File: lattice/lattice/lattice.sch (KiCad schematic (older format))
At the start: 108 parts, among them J1 AudioJack2, J10 AudioJack2, J11 AudioJack2, J12 AudioJack2, J13 AudioJack2, J14 AudioJack2, J15 AudioJack2, J16 Conn_02x05_Odd_Even, J17 Conn_01x10, J18 Conn_01x10, J19 Conn_01x08, J2 AudioJack2, J20 Conn_01x08, J21 Conn_01x07, J22 Conn_01x07, J23 Conn_01x07, J24 Conn_01x07, J3 AudioJack2, J4 AudioJack2, J5 AudioJack2, J6 AudioJack2, J7 AudioJack2, J8 AudioJack2, J9 Conn_02x08_Odd_Even, Q1 BC548, Q2 BC548, SW1 LP4OA1PBCT, U1 MCP6002-xP, U2 MCP6002-xP, U3 MCP6002-xP, U5 6N138, U6 LM4040LP-5, U7 74HC595

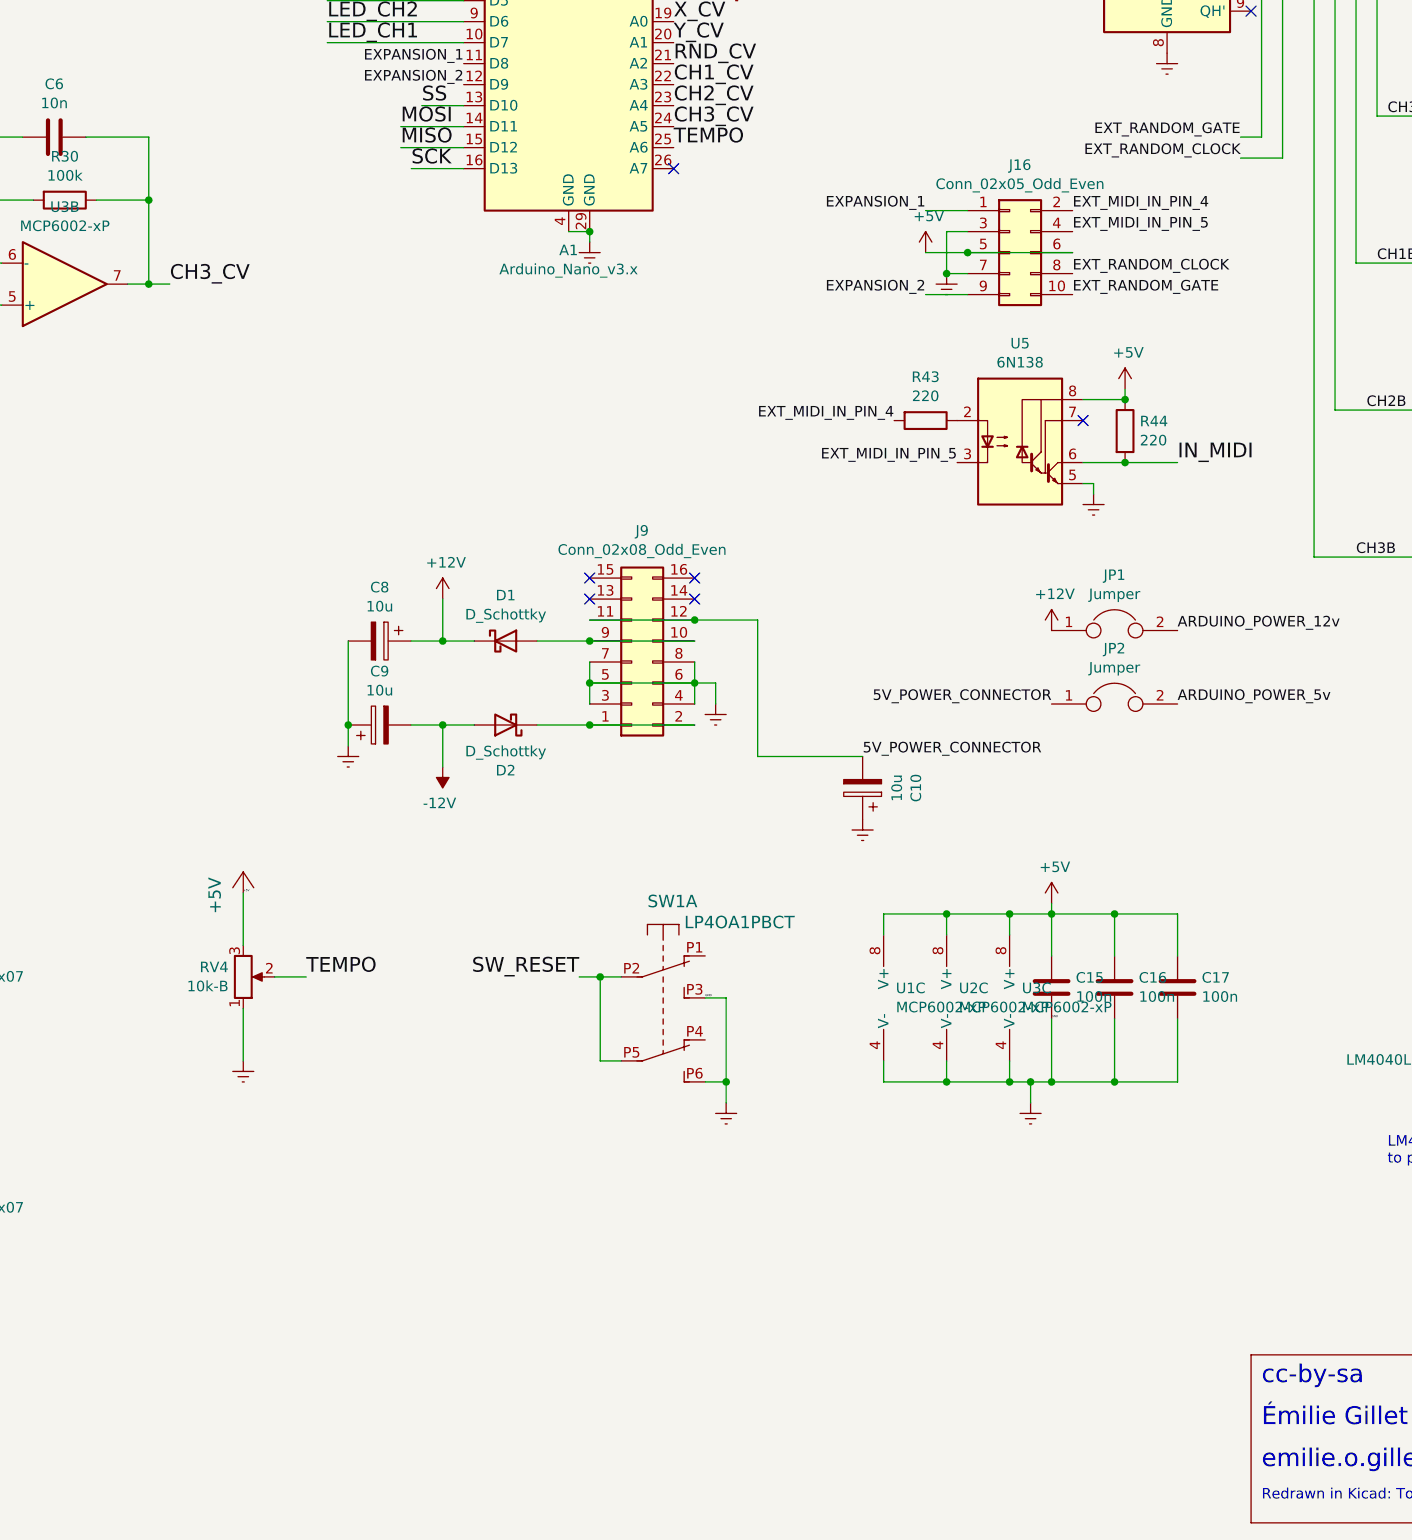
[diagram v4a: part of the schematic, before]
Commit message: Adding expansion board
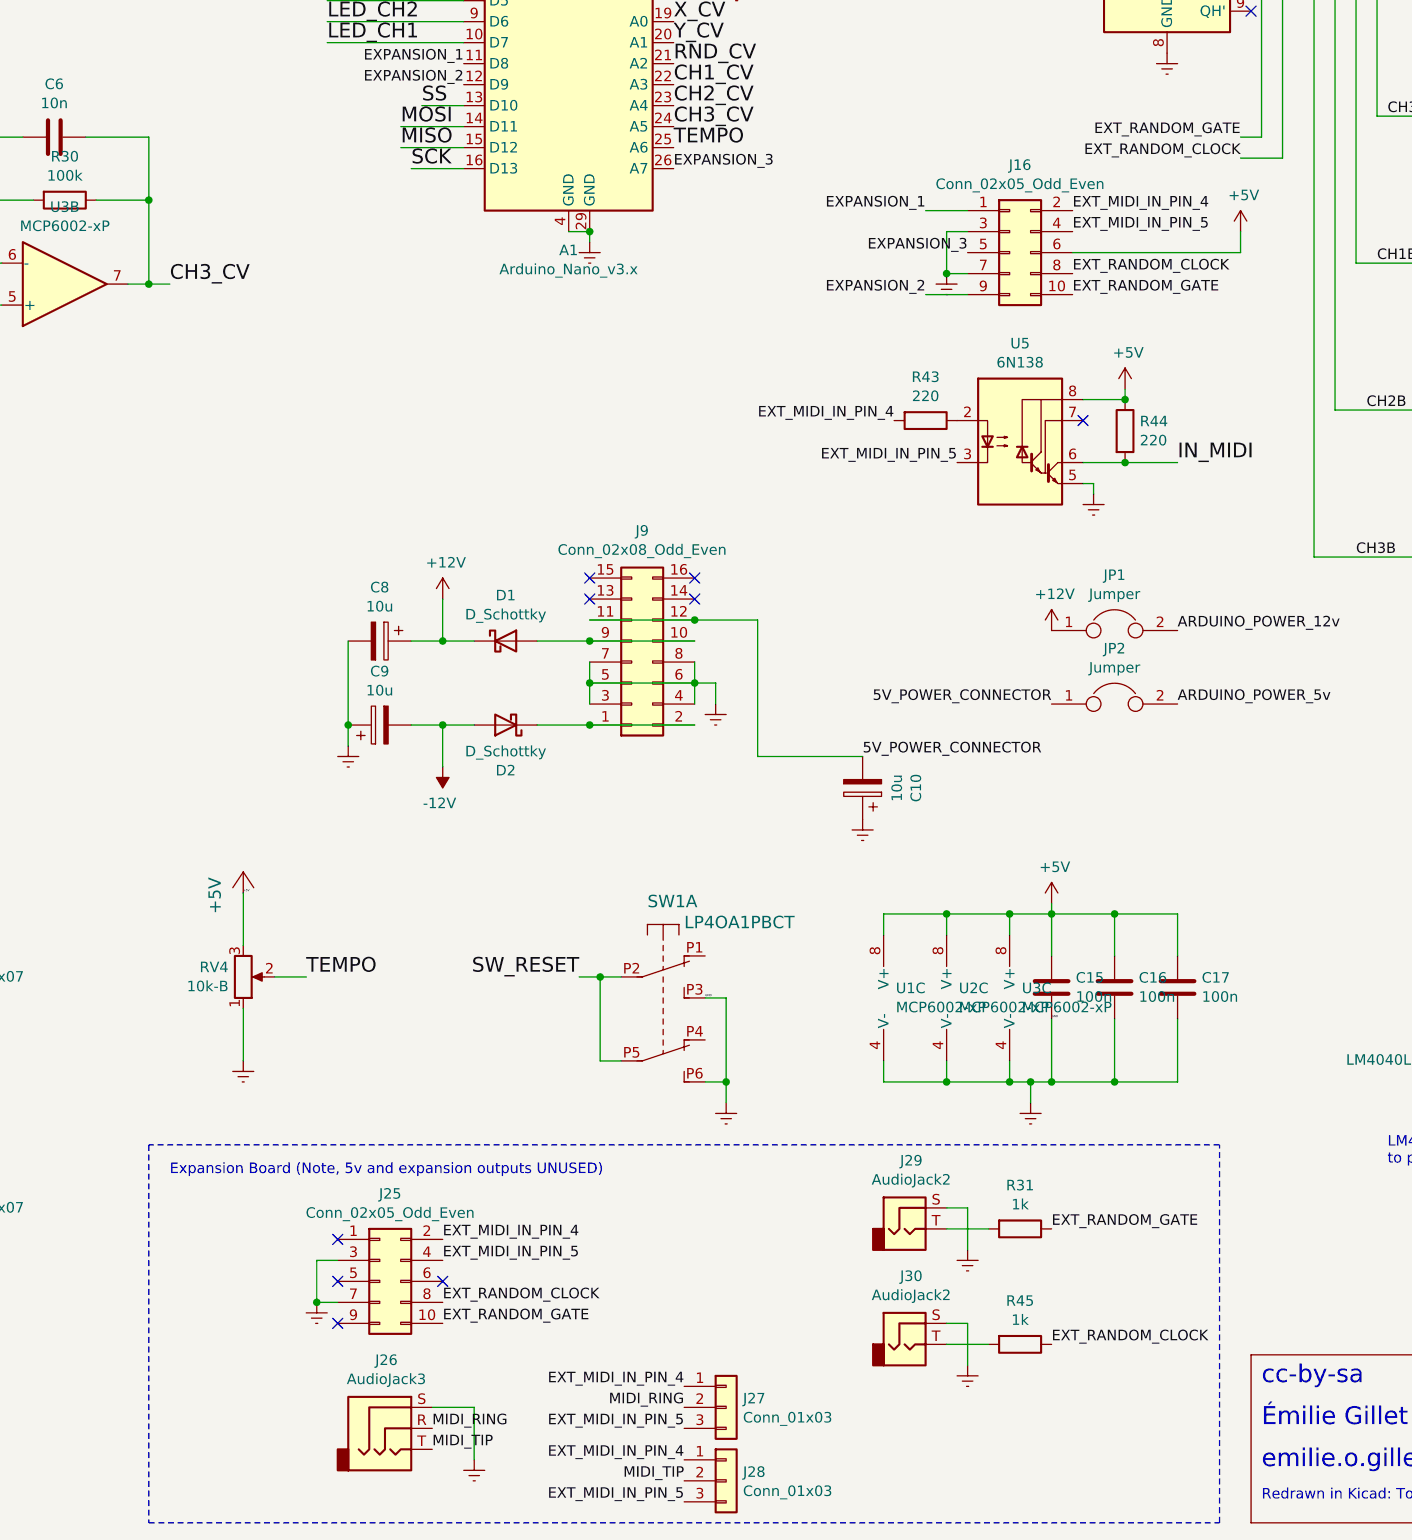
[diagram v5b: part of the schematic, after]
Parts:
- added J25: Conn_02x05_Odd_Even, Connector_PinHeader_2.54mm:PinHeader_2x05_P2.54mm_Vertical, symbol Connector_Generic:Conn_02x05_Odd_Even
- added J26: AudioJack3, RS:Jack_3.5mm_QingPu_WQP-PJ398SM_Vertical_CircularHoles, symbol Connector:AudioJack3
- added J27, J28: Conn_01x03, Connector_PinHeader_2.54mm:PinHeader_1x03_P2.54mm_Vertical, symbol Connector_Generic:Conn_01x03
- added J29, J30: AudioJack2, Connector_Audio:Jack_3.5mm_QingPu_WQP-PJ398SM_Vertical_CircularHoles, symbol Connector:AudioJack2
- added R31, R45: 1k, Resistor_THT:R_Axial_DIN0207_L6.3mm_D2.5mm_P7.62mm_Horizontal, symbol Device:R
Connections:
- net +5V: no longer J16.5 (Pin_5)
- net EXT_MIDI_IN_PIN_4: now also J25.2 (Pin_2), J27.1 (Pin_1), J28.1 (Pin_1)
- net EXT_MIDI_IN_PIN_5: now also J25.4 (Pin_4), J27.3 (Pin_3), J28.3 (Pin_3)
- net EXT_RANDOM_CLOCK: now also J25.8 (Pin_8), R45.1
- net EXT_RANDOM_GATE: now also J25.10 (Pin_10), R31.1
- net Earth: now also J25.3 (Pin_3), J25.7 (Pin_7), J26.S, J29.S, J30.S
- net EXPANSION_3: now reaches A1.26 (A7)
- net EXPANSION_3: now also J16.5 (Pin_5)
- new net: J29.T, R31.2
- new net: J30.T, R45.2
- new net MIDI_RING: J26.R, J27.2 (Pin_2)
- new net MIDI_TIP: J26.T, J28.2 (Pin_2)
- no-connect marks 8 -> 11
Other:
- note added: "Expansion Board (Note, 5v and expansion outputs UNUSED)"
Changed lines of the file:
@@
 	1    0    0    -1
 $EndComp
-NoConn ~ 10250 4950
 NoConn ~ 9850 3250
 NoConn ~ 13000 4200
@@
 L power:+5V #PWR0137
 U 1 1 615A568E
-P 11450 5350
-F 0 "#PWR0137" H 11450 5200 50  0001 C CNN
-F 1 "+5V" H 11465 5523 50  0000 C CNN
-F 2 "" H 11450 5350 50  0001 C CNN
-F 3 "" H 11450 5350 50  0001 C CNN
-	1    11450 5350
+P 12950 5250
+F 0 "#PWR0137" H 12950 5100 50  0001 C CNN
+F 1 "+5V" H 12965 5423 50  0000 C CNN
+F 2 "" H 12950 5250 50  0001 C CNN
+F 3 "" H 12950 5250 50  0001 C CNN
+	1    12950 5250
 	1    0    0    -1
 $EndComp
@@
 	1    0    0    -1
 $EndComp
-Wire Wire Line
-	11450 5350 11650 5350
 $Comp
 L Device:C C11
@@
 Wire Notes Line
 	16100 3050 16100 4950
-Wire Wire Line
-	12150 5350 11650 5350
-Connection ~ 11650 5350
 Text Label 9250 4450 2    50   ~ 0
 EXPANSION_1
@@
 Wire Wire Line
 	11450 5150 11650 5150
+Text Label 10250 4950 0    50   ~ 0
+EXPANSION_3
+Text Label 11650 5350 2    50   ~ 0
+EXPANSION_3
+Wire Wire Line
+	12950 5250 12950 5350
+Wire Wire Line
+	12950 5350 12150 5350
+Wire Notes Line
+	12850 11400 12850 9600
+Wire Notes Line
+	12850 9600 7750 9600
+Wire Notes Line
+	7750 9600 7750 11400
+Wire Notes Line
+	7750 11400 12850 11400
+Text Notes 7850 9750 0    50   ~ 0
+Expansion Board (Note, 5v and expansion outputs UNUSED)
+Text Label 9150 10050 0    50   ~ 0
+EXT_MIDI_IN_PIN_4
+Text Label 9150 10150 0    50   ~ 0
+EXT_MIDI_IN_PIN_5
+Text Label 9150 10450 0    50   ~ 0
+EXT_RANDOM_GATE
+Text Label 9150 10350 0    50   ~ 0
+EXT_RANDOM_CLOCK
+$Comp
+L power:Earth #PWR0176
+U 1 1 61A00EAF
+P 8550 10350
+F 0 "#PWR0176" H 8550 10100 50  0001 C CNN
+F 1 "Earth" H 8550 10200 50  0001 C CNN
+F 2 "" H 8550 10350 50  0001 C CNN
+F 3 "~" H 8550 10350 50  0001 C CNN
+	1    8550 10350
+	1    0    0    -1
+$EndComp
+Wire Wire Line
+	8650 10150 8550 10150
+Wire Wire Line
+	8550 10150 8550 10350
+Wire Wire Line
+	8550 10350 8650 10350
+$Comp
+L Connector_Generic:Conn_02x05_Odd_Even J25
+U 1 1 61A00EB8
+P 8850 10250
+F 0 "J25" H 8900 10667 50  0000 C CNN
+F 1 "Conn_02x05_Odd_Even" H 8900 10576 50  0000 C CNN
+F 2 "Connector_PinHeader_2.54mm:PinHeader_2x05_P2.54mm_Vertical" H 8850 10250 50  0001 C CNN
+F 3 "~" H 8850 10250 50  0001 C CNN
+	1    8850 10250
+	1    0    0    -1
+$EndComp
+Connection ~ 8550 10350
+NoConn ~ 9150 10250
+Wire Wire Line
+	11550 9900 11650 9900
+$Comp
+L Connector:AudioJack2 J29
+U 1 1 61A780B5
+P 11350 10000
+F 0 "J29" H 11382 10325 50  0000 C CNN
+F 1 "AudioJack2" H 11382 10234 50  0000 C CNN
+F 2 "Connector_Audio:Jack_3.5mm_QingPu_WQP-PJ398SM_Vertical_CircularHoles" H 11350 10000 50  0001 C CNN
+F 3 "~" H 11350 10000 50  0001 C CNN
+	1    11350 10000
+	1    0    0    -1
+$EndComp
+$Comp
+L power:Earth #PWR0177
+U 1 1 61A780BB
+P 11650 10100
+F 0 "#PWR0177" H 11650 9850 50  0001 C CNN
+F 1 "Earth" H 11650 9950 50  0001 C CNN
+F 2 "" H 11650 10100 50  0001 C CNN
+F 3 "~" H 11650 10100 50  0001 C CNN
+	1    11650 10100
+	1    0    0    -1
+$EndComp
+Wire Wire Line
+	11750 10000 11550 10000
+$Comp
+L Device:R R31
+U 1 1 61A954F0
+P 11900 10000
+F 0 "R31" V 11693 10000 50  0000 C CNN
+F 1 "1k" V 11784 10000 50  0000 C CNN
+F 2 "Resistor_THT:R_Axial_DIN0207_L6.3mm_D2.5mm_P7.62mm_Horizontal" V 11830 10000 50  0001 C CNN
+F 3 "~" H 11900 10000 50  0001 C CNN
+	1    11900 10000
+	0    1    1    0
+$EndComp
+Text Label 12050 10000 0    50   ~ 0
+EXT_RANDOM_GATE
+Wire Wire Line
+	11650 10100 11650 9900
+Wire Wire Line
+	11550 10450 11650 10450
+$Comp
+L Connector:AudioJack2 J30
+U 1 1 61B4508F
+P 11350 10550
+F 0 "J30" H 11382 10875 50  0000 C CNN
+F 1 "AudioJack2" H 11382 10784 50  0000 C CNN
+F 2 "Connector_Audio:Jack_3.5mm_QingPu_WQP-PJ398SM_Vertical_CircularHoles" H 11350 10550 50  0001 C CNN
+F 3 "~" H 11350 10550 50  0001 C CNN
+	1    11350 10550
+	1    0    0    -1
+$EndComp
+$Comp
+L power:Earth #PWR0178
+U 1 1 61B45095
+P 11650 10650
+F 0 "#PWR0178" H 11650 10400 50  0001 C CNN
+F 1 "Earth" H 11650 10500 50  0001 C CNN
+F 2 "" H 11650 10650 50  0001 C CNN
+F 3 "~" H 11650 10650 50  0001 C CNN
+	1    11650 10650
+	1    0    0    -1
+$EndComp
+Wire Wire Line
+	11750 10550 11550 10550
+$Comp
+L Device:R R45
+U 1 1 61B4509C
+P 11900 10550
+F 0 "R45" V 11693 10550 50  0000 C CNN
+F 1 "1k" V 11784 10550 50  0000 C CNN
+F 2 "Resistor_THT:R_Axial_DIN0207_L6.3mm_D2.5mm_P7.62mm_Horizontal" V 11830 10550 50  0001 C CNN
+F 3 "~" H 11900 10550 50  0001 C CNN
+	1    11900 10550
+	0    1    1    0
+$EndComp
+Text Label 12050 10550 0    50   ~ 0
+EXT_RANDOM_CLOCK
+Wire Wire Line
+	11650 10650 11650 10450
+$Comp
+L power:Earth #PWR0179
+U 1 1 61BA04ED
+P 9300 11100
+F 0 "#PWR0179" H 9300 10850 50  0001 C CNN
+F 1 "Earth" H 9300 10950 50  0001 C CNN
+F 2 "" H 9300 11100 50  0001 C CNN
+F 3 "~" H 9300 11100 50  0001 C CNN
+	1    9300 11100
+	1    0    0    -1
+$EndComp
+Wire Wire Line
+	9300 10850 9300 11100
+$Comp
+L Connector:AudioJack3 J26
+U 1 1 61C1C65B
+P 8900 10950
+F 0 "J26" H 8882 11275 50  0000 C CNN
+F 1 "AudioJack3" H 8882 11184 50  0000 C CNN
+F 2 "RS:Jack_3.5mm_QingPu_WQP-PJ398SM_Vertical_CircularHoles" H 8900 10950 50  0001 C CNN
+F 3 "~" H 8900 10950 50  0001 C CNN
+	1    8900 10950
+	1    0    0    -1
+$EndComp
+Wire Wire Line
+	9100 10850 9300 10850
+$Comp
+L Connector_Generic:Conn_01x03 J27
+U 1 1 61C5B500
+P 10500 10850
+F 0 "J27" H 10580 10892 50  0000 L CNN
+F 1 "Conn_01x03" H 10580 10801 50  0000 L CNN
+F 2 "Connector_PinHeader_2.54mm:PinHeader_1x03_P2.54mm_Vertical" H 10500 10850 50  0001 C CNN
+F 3 "~" H 10500 10850 50  0001 C CNN
+	1    10500 10850
+	1    0    0    -1
+$EndComp
+$Comp
+L Connector_Generic:Conn_01x03 J28
+U 1 1 61C5DAC0
+P 10500 11200
+F 0 "J28" H 10580 11242 50  0000 L CNN
+F 1 "Conn_01x03" H 10580 11151 50  0000 L CNN
+F 2 "Connector_PinHeader_2.54mm:PinHeader_1x03_P2.54mm_Vertical" H 10500 11200 50  0001 C CNN
+F 3 "~" H 10500 11200 50  0001 C CNN
+	1    10500 11200
+	1    0    0    -1
+$EndComp
+Text Label 9100 11050 0    50   ~ 0
+MIDI_TIP
+Text Label 9100 10950 0    50   ~ 0
+MIDI_RING
+Text Label 10300 10850 2    50   ~ 0
+MIDI_RING
+Text Label 10300 11200 2    50   ~ 0
+MIDI_TIP
+Text Label 10300 10750 2    50   ~ 0
+EXT_MIDI_IN_PIN_4
+Text Label 10300 10950 2    50   ~ 0
+EXT_MIDI_IN_PIN_5
+Text Label 10300 11100 2    50   ~ 0
+EXT_MIDI_IN_PIN_4
+Text Label 10300 11300 2    50   ~ 0
+EXT_MIDI_IN_PIN_5
+NoConn ~ 8650 10050
+NoConn ~ 8650 10250
+NoConn ~ 8650 10450
 $EndSCHEMATC
